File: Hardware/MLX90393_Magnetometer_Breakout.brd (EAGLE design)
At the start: 25.4 x 23.5 mm, 16 parts, among them U1 MLX90393_MAGNETOMETER

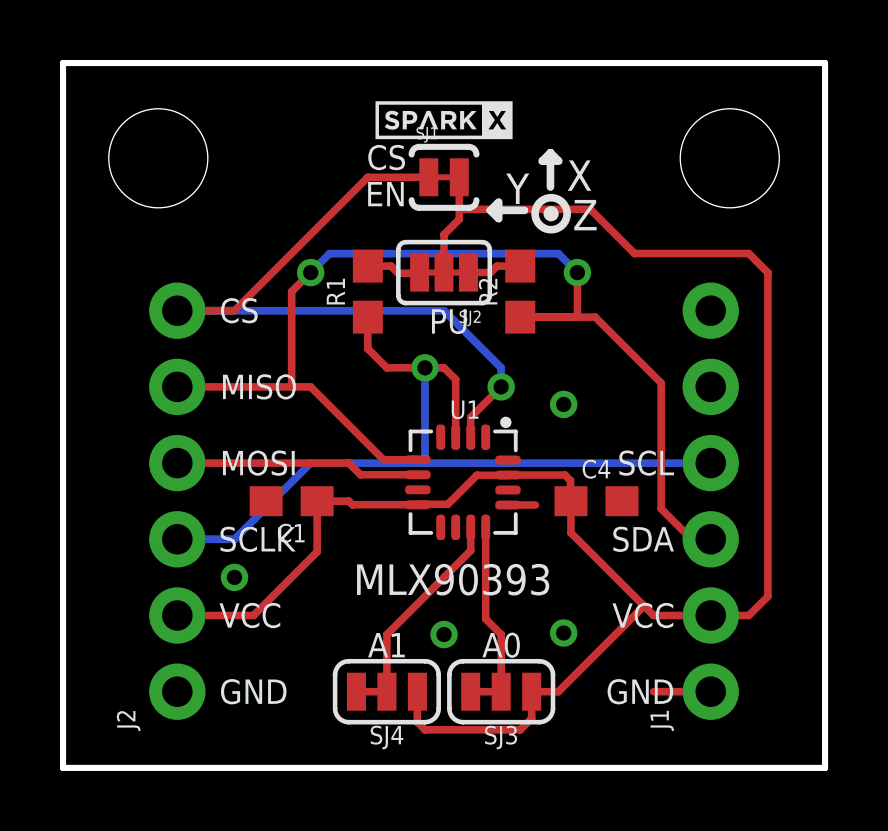
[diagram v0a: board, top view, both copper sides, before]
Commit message: Production layout and panel for review
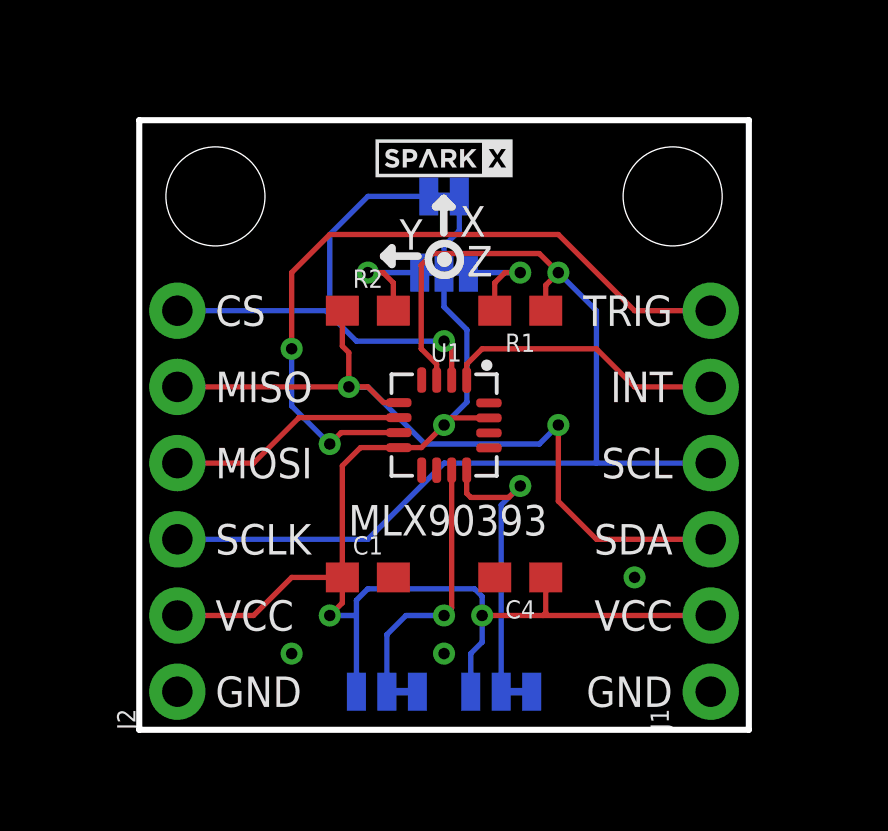
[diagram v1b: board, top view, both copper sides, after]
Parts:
- SJ1: device SparkFun:SJ_2S-TRACE -> SparkFun-Jumpers:SMT-JUMPER_2_NC_TRACE_SILK
- moved U$1 24.5 mm to (10.2, 6.35)
- moved R1 5.12 mm to (12.7, 14.0), turned to 180 degrees
- moved R2 5.12 mm to (7.62, 14.0), turned to 0 degrees
- moved C4 3.59 mm to (12.7, 5.08), turned to 180 degrees
- moved C1 3.59 mm to (7.62, 5.08), turned to 0 degrees
- moved JP3 2.29 mm to (2.54, 17.8)
- moved JP4 2.29 mm to (17.8, 17.8)
- moved U1 2.01 mm to (10.2, 10.2)
- moved U$2 1.27 mm to (10.2, 19.1)
- moved SJ1 0.63 mm to (10.2, 17.8), flipped to the bottom, turned to 180 degrees
- flipped SJ2 to the bottom
- flipped SJ3 to the bottom
- flipped SJ4 to the bottom
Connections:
- net VDD renamed 3.3V
- net INT: now also J1.5
- net TRIG: now also J1.6
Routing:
- net TRIG: track 0.00 -> 24.2 mm, vias 0 -> 2
- net 3.3V: track 62.2 -> 45.9 mm, vias 0 -> 3
- net SDA: track 37.8 -> 26.4 mm
- net INT: track 0.00 -> 9.40 mm
- net SCL: track 28.3 -> 36.2 mm
- net CS: track 24.5 -> 17.2 mm
- net A0: track 5.69 -> 9.89 mm, vias 0 -> 1
- net GND: track 2.79 -> 0.00 mm, vias 4 -> 3
- net A1: track 6.64 -> 9.02 mm, vias 0 -> 1
- net N$4: track 1.82 -> 3.65 mm, vias 0 -> 1
- net N$5: track 1.84 -> 3.65 mm, vias 0 -> 1
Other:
- board size 25.4 x 23.5 mm -> 20.3 x 20.3 mm
- board text added: "INT"
- board text added: "J. Bartlett"
- board text added: "TRIG"
- board text removed: "CS EN"

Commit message: Adding bottom silk
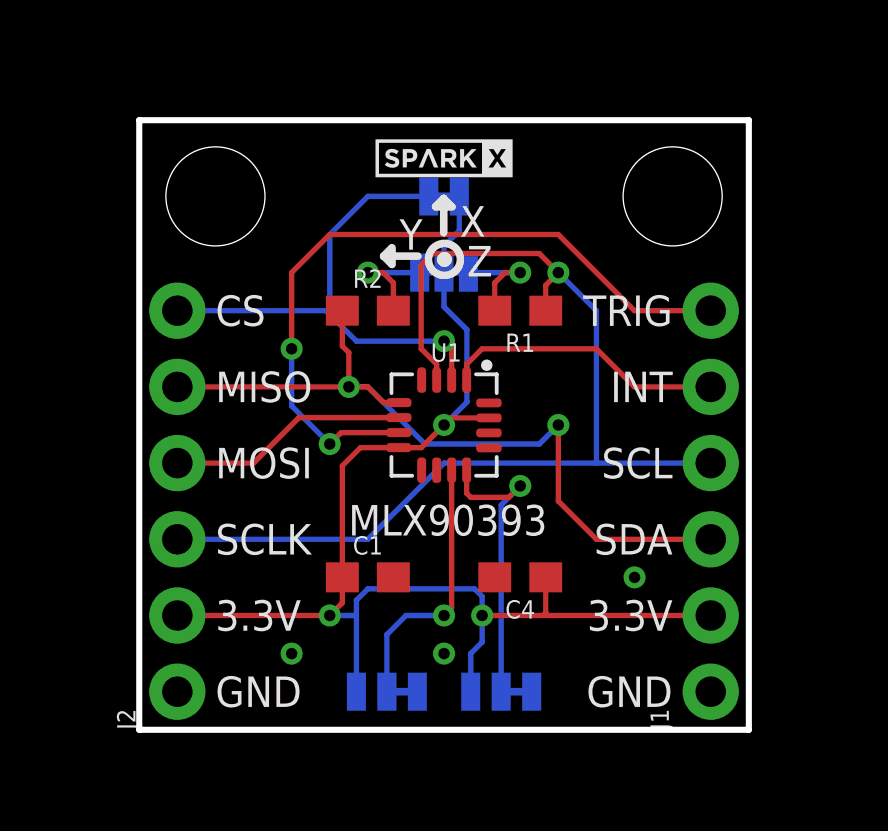
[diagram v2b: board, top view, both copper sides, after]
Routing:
- net 3.3V: track 45.9 -> 44.9 mm
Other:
- board text added: "3.3V"
- board text removed: "VCC"
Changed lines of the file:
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@@
 <wire x1="0" y1="20.32" x2="20.32" y2="20.32" width="0.2032" layer="20"/>
 <wire x1="20.32" y1="20.32" x2="20.32" y2="0" width="0.2032" layer="20"/>
-<text x="17.78" y="3.302" size="1.016" layer="21" font="vector" ratio="15" align="bottom-right">VCC</text>
+<text x="17.78" y="3.302" size="1.016" layer="21" font="vector" ratio="15" align="bottom-right">3.3V</text>
 <text x="17.78" y="5.842" size="1.016" layer="21" font="vector" ratio="15" distance="15" align="bottom-right">SDA</text>
 <text x="17.78" y="8.382" size="1.016" layer="21" font="vector" ratio="15" align="bottom-right">SCL</text>
@@
 <wire x1="8.42645" y1="15.509875" x2="8.42645" y2="16.068675" width="0.254" layer="21"/>
 <text x="2.54" y="0.762" size="1.016" layer="21" font="vector" ratio="15" rot="SR0">GND</text>
-<text x="2.54" y="3.302" size="1.016" layer="21" font="vector" ratio="15" rot="SR0">VCC</text>
+<text x="2.54" y="3.302" size="1.016" layer="21" font="vector" ratio="15" rot="SR0">3.3V</text>
 <text x="2.54" y="5.842" size="1.016" layer="21" font="vector" ratio="15">SCLK</text>
 <text x="2.54" y="8.382" size="1.016" layer="21" font="vector" ratio="15">MOSI</text>
@@
 <text x="17.78" y="13.462" size="1.016" layer="21" font="vector" ratio="15" align="bottom-right">TRIG</text>
 <text x="10.16" y="-10.16" size="1.778" layer="51" font="vector" ratio="15">J. Bartlett</text>
+<text x="4.191" y="13.462" size="1.016" layer="22" font="vector" ratio="15" rot="MR0">CS</text>
+<text x="5.715" y="10.922" size="1.016" layer="22" font="vector" ratio="15" rot="MR0">MISO</text>
+<text x="5.715" y="8.382" size="1.016" layer="22" font="vector" ratio="15" rot="MR0">MOSI</text>
+<text x="6.096" y="5.842" size="1.016" layer="22" font="vector" ratio="15" rot="MR0">SCLK</text>
+<text x="5.715" y="3.302" size="1.016" layer="22" font="vector" ratio="15" rot="SMR0">3.3V</text>
+<text x="5.08" y="0.762" size="1.016" layer="22" font="vector" ratio="15" rot="SMR0">GND</text>
+<text x="14.859" y="0.762" size="1.016" layer="22" font="vector" ratio="15" rot="MR0" align="bottom-right">GND</text>
+<text x="14.351" y="3.302" size="1.016" layer="22" font="vector" ratio="15" rot="MR0" align="bottom-right">3.3V</text>
+<text x="14.859" y="5.842" size="1.016" layer="22" font="vector" ratio="15" distance="15" rot="MR0" align="bottom-right">SDA</text>
+<text x="14.859" y="8.382" size="1.016" layer="22" font="vector" ratio="15" rot="MR0" align="bottom-right">SCL</text>
+<text x="15.24" y="10.922" size="1.016" layer="22" font="vector" ratio="15" rot="MR0" align="bottom-right">INT</text>
+<text x="14.224" y="13.462" size="1.016" layer="22" font="vector" ratio="15" rot="MR0" align="bottom-right">TRIG</text>
 </plain>
 <attributes>
@@
 <wire x1="7.374" y1="9.406" x2="6.77" y2="8.802" width="0.1778" layer="1"/>
 <wire x1="6.77" y1="5.08" x2="6.77" y2="8.802" width="0.1778" layer="1"/>
-<wire x1="6.77" y1="5.08" x2="5.08" y2="5.08" width="0.1778" layer="1"/>
-<wire x1="5.08" y1="5.08" x2="3.81" y2="3.81" width="0.1778" layer="1"/>
-<wire x1="3.81" y1="3.81" x2="1.27" y2="3.81" width="0.1778" layer="1"/>
 <wire x1="6.77" y1="5.08" x2="6.77" y2="4.23" width="0.1778" layer="1"/>
 <via x="6.35" y="3.81" extent="1-16" drill="0.381"/>
@@
 <wire x1="11.049" y1="2.54" x2="11.43" y2="2.921" width="0.1778" layer="16"/>
 <wire x1="11.43" y1="2.921" x2="11.43" y2="3.81" width="0.1778" layer="16"/>
+<wire x1="1.27" y1="3.81" x2="6.35" y2="3.81" width="0.1778" layer="1"/>
 </signal>
 </signals>
